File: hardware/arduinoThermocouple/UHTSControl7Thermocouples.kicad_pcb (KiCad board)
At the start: 2 copper layers, 141.6 x 63.5 mm, 71 parts, among them J1 Conn_01x12, J2 Conn_01x02, J3 Conn_01x02, J4 Conn_01x02, J5 Conn_01x02, J6 Conn_01x02, J7 Conn_01x02, J8 Conn_01x02, U1 LM317L_TO92, U2 MAX31856MUD+, U3 MAX31856MUD+, U4 MAX31856MUD+, U5 MAX31856MUD+, U6 MAX31856MUD+, U7 MAX31856MUD+, U8 MAX31856MUD+

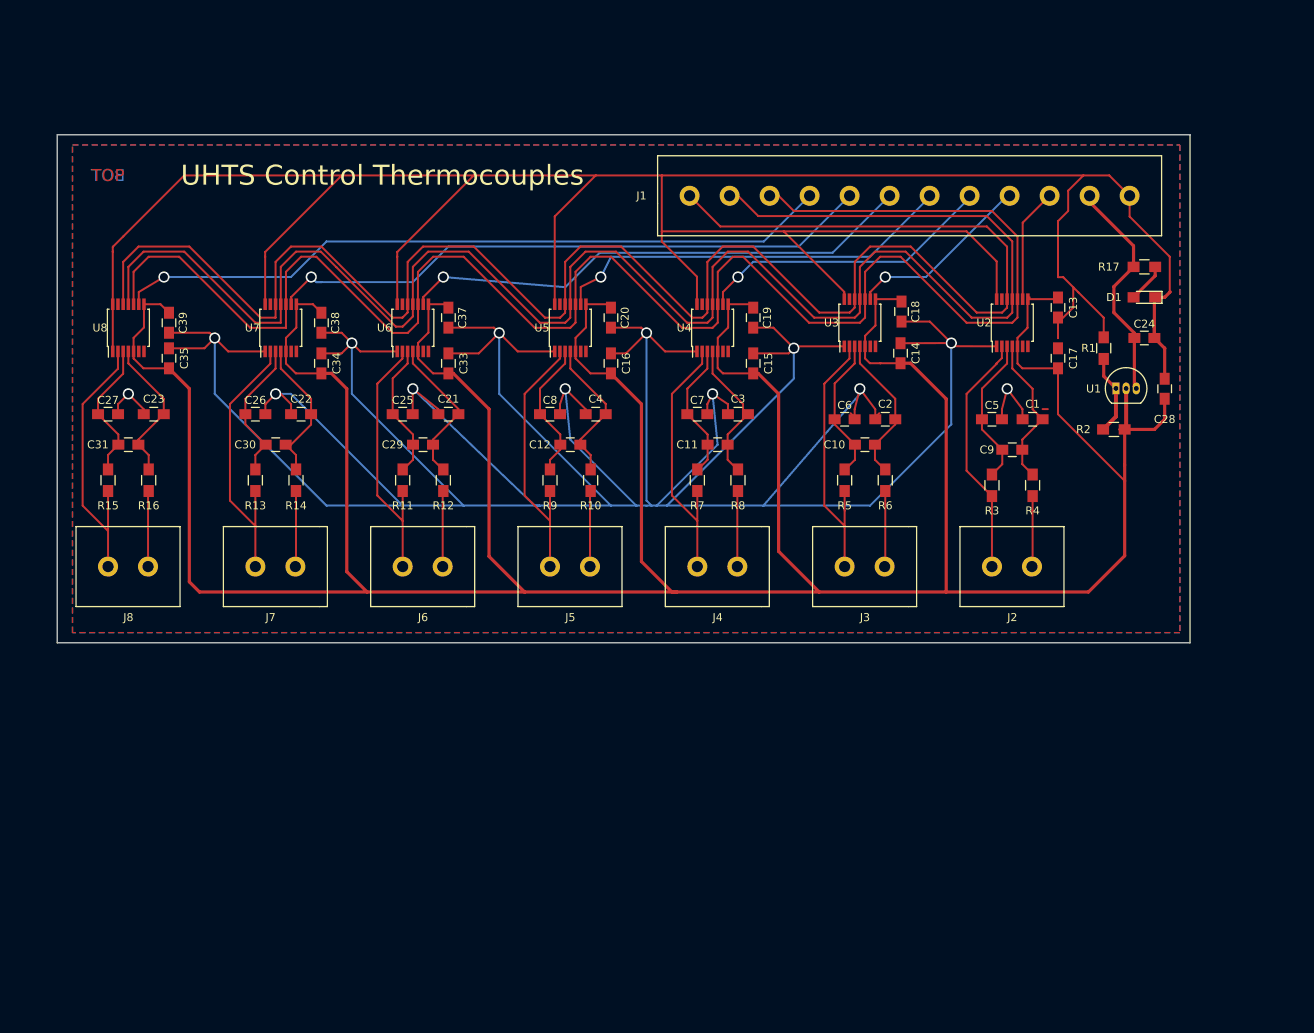
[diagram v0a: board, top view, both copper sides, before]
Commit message: Trying to learn python scripting in KiCad.
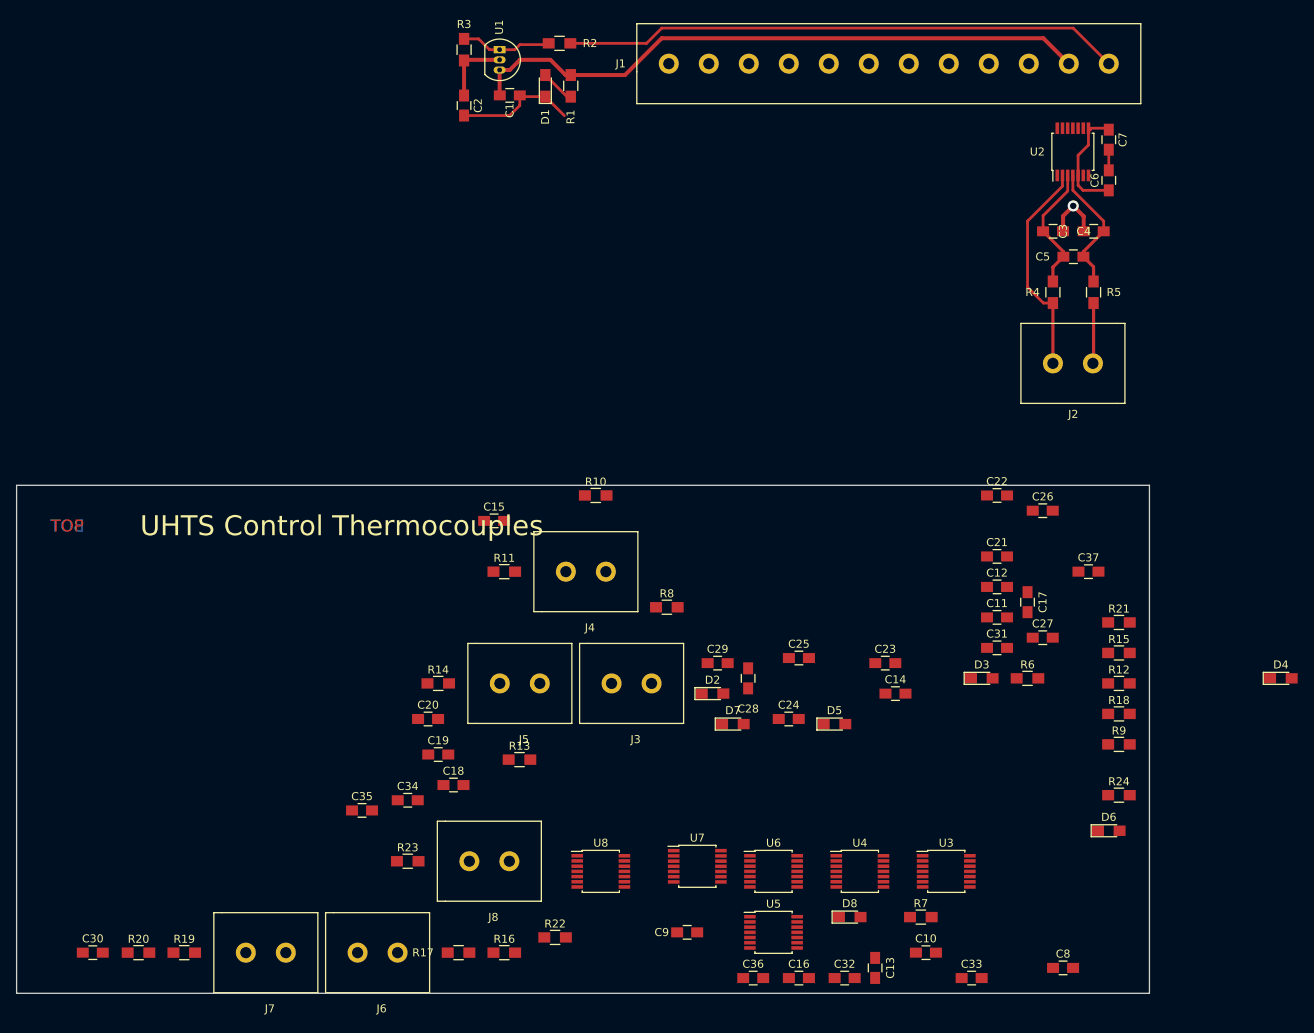
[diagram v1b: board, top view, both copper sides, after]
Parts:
- removed C38, C39: 0.1u, Capacitors_SMD:C_0805_HandSoldering
- added C32: 0.1u, Capacitors_SMD:C_0805_HandSoldering, F.Cu at (205.1, 139.1)
- added C36: 0.1u, Capacitors_SMD:C_0805_HandSoldering, F.Cu at (193.7, 139.1)
- added D2: LED, LEDs:LED_0805_HandSoldering, F.Cu at (188.6, 103.5)
- added D3: LED, LEDs:LED_0805_HandSoldering, F.Cu at (222.2, 101.6)
- added D4: LED, LEDs:LED_0805_HandSoldering, F.Cu at (259.6, 101.6)
- added D5: LED, LEDs:LED_0805_HandSoldering, F.Cu at (203.8, 107.3)
- added D6: LED, LEDs:LED_0805_HandSoldering, F.Cu at (238.1, 120.7)
- added D7: LED, LEDs:LED_0805_HandSoldering, F.Cu at (191.1, 107.3)
- added D8: LED, LEDs:LED_0805_HandSoldering, F.Cu at (205.7, 131.4)
- added R18: R, Resistors_SMD:R_0805_HandSoldering, F.Cu at (239.4, 106.0)
- added R19: 100, Resistors_SMD:R_0805_HandSoldering, F.Cu at (122.6, 135.9)
- added R20: 100, Resistors_SMD:R_0805_HandSoldering, F.Cu at (116.8, 135.9)
- added R21: R, Resistors_SMD:R_0805_HandSoldering, F.Cu at (239.4, 94.6)
- added R22: 100, Resistors_SMD:R_0805_HandSoldering, F.Cu at (168.9, 134.0)
- added R23: 100, Resistors_SMD:R_0805_HandSoldering, F.Cu at (150.5, 124.5)
- added R24: R, Resistors_SMD:R_0805_HandSoldering, F.Cu at (239.4, 116.2)
- C1: value 0.01u -> 0.1uF
- C13, C14, C18, C19, C29, C33, C34, C9: value 0.1u -> 0.01u
- C2: value 0.01u -> 1uF
- C21, C22, C25, C26, C27, C5, C6, C7: value 0.01u -> 0.1u
- C24: value 0.1uF -> 0.01u
- C28: value 1uF -> 0.01u
- R1: value 560 -> 820
- R17: value 820 -> 100
- R2: value 330 -> 560
- R3: value 100 -> 330
- moved R15 128.2 mm to (239.4, 98.4), turned to 0 degrees
- moved R17 121.2 mm to (156.8, 135.9)
- moved C27 120.1 mm to (229.9, 96.5)
- moved C31 111.5 mm to (224.2, 97.8)
- moved C33 100.9 mm to (221.0, 139.1), turned to 0 degrees
- moved C26 99.2 mm to (229.9, 80.6)
- moved C23 96.6 mm to (210.2, 99.7), turned to 0 degrees
- moved C8 94.4 mm to (232.4, 137.8)
- moved U8 90.0 mm to (174.6, 125.7), turned to 0 degrees
- moved R12 88.2 mm to (239.4, 102.2), turned to 0 degrees
- moved U1 87.9 mm to (162.0, 23.0), turned to 270 degrees
- moved C22 87.6 mm to (224.2, 78.7), turned to 0 degrees
- moved C37 86.1 mm to (235.6, 88.3), turned to 0 degrees
- moved C13 85.7 mm to (208.9, 137.8)
- moved R3 85.6 mm to (157.5, 23.0), turned to 90 degrees
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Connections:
- C1 pad 1: Net-(C1-Pad1) -> +VSW
- C11 pad 1: Net-(C11-Pad1) -> +3V3
- C11 pad 2: Net-(C11-Pad2) -> GND
- C12 pad 1: Net-(C12-Pad1) -> +3V3
- C12 pad 2: Net-(C12-Pad2) -> GND
- C13 pad 1: +3V3 -> Net-(C13-Pad1)
- C14 pad 1: +3V3 -> Net-(C14-Pad1)
- C15 pad 1: +3V3 -> Net-(C14-Pad1)
- C15 pad 2: GND -> Net-(C13-Pad1)
- C18 pad 1: +3V3 -> Net-(C18-Pad1)
- C19 pad 1: +3V3 -> Net-(C19-Pad1)
- C2 pad 1: Net-(C10-Pad2) -> +3V3
- C20 pad 1: +3V3 -> Net-(C19-Pad1)
- C20 pad 2: GND -> Net-(C18-Pad1)
- C21 pad 1: Net-(C21-Pad1) -> +3V3
- C22 pad 1: Net-(C22-Pad1) -> +3V3
- C24 pad 1: +VSW -> Net-(C24-Pad1)
- C25 pad 1: Net-(C25-Pad1) -> Net-(C24-Pad1)
- C25 pad 2: GND -> Net-(C23-Pad1)
- C26 pad 1: Net-(C26-Pad1) -> +3V3
- C27 pad 1: Net-(C27-Pad1) -> +3V3
- C28 pad 1: +3V3 -> Net-(C28-Pad1)
- C29 pad 1: Net-(C25-Pad1) -> Net-(C29-Pad1)
- C29 pad 2: Net-(C21-Pad1) -> GND
- C3 pad 1: Net-(C11-Pad2) -> Net-(C3-Pad1)
- C30 pad 1: Net-(C26-Pad1) -> Net-(C29-Pad1)
- C30 pad 2: Net-(C22-Pad1) -> Net-(C28-Pad1)
- C31 pad 1: Net-(C27-Pad1) -> +3V3
- C31 pad 2: Net-(C23-Pad1) -> GND
- C33 pad 1: +3V3 -> Net-(C33-Pad1)
- C34 pad 1: +3V3 -> Net-(C34-Pad1)
- C35 pad 1: +3V3 -> Net-(C34-Pad1)
- C35 pad 2: GND -> Net-(C33-Pad1)
- C4 pad 1: Net-(C12-Pad2) -> Net-(C4-Pad1)
- C5 pad 1: Net-(C5-Pad1) -> Net-(C4-Pad1)
- C5 pad 2: GND -> Net-(C3-Pad1)
- C6 pad 1: Net-(C10-Pad1) -> +3V3
- C7 pad 1: Net-(C11-Pad1) -> +3V3
- C8 pad 1: Net-(C12-Pad1) -> Net-(C10-Pad2)
- C9 pad 1: Net-(C5-Pad1) -> Net-(C10-Pad1)
- C9 pad 2: Net-(C1-Pad1) -> GND
- R1 pad 1: Net-(R1-Pad1) -> +VSW
- R1 pad 2: GND -> Net-(D1-Pad2)
- R10 pad 1: Net-(C12-Pad2) -> Net-(C19-Pad1)
- R10 pad 2: Net-(J5-Pad1) -> Net-(J5-Pad2)
- R11 pad 1: Net-(C25-Pad1) -> Net-(C18-Pad1)
- R11 pad 2: Net-(J6-Pad2) -> Net-(J5-Pad1)
- R12 pad 1: Net-(C21-Pad1) -> Net-(C24-Pad1)
- R12 pad 2: Net-(J6-Pad1) -> Net-(J6-Pad2)
- R13 pad 1: Net-(C26-Pad1) -> Net-(C23-Pad1)
- R13 pad 2: Net-(J7-Pad2) -> Net-(J6-Pad1)
- R14 pad 1: Net-(C22-Pad1) -> Net-(C29-Pad1)
- R14 pad 2: Net-(J7-Pad1) -> Net-(J7-Pad2)
- R15 pad 1: Net-(C27-Pad1) -> Net-(C28-Pad1)
- R15 pad 2: Net-(J8-Pad2) -> Net-(J7-Pad1)
- R16 pad 1: Net-(C23-Pad1) -> Net-(C34-Pad1)
- R16 pad 2: Net-(J8-Pad1) -> Net-(J8-Pad2)
- R17 pad 1: +VSW -> Net-(C33-Pad1)
- R17 pad 2: Net-(D1-Pad2) -> Net-(J8-Pad1)
- R2 pad 1: +3V3 -> Net-(R2-Pad1)
- R2 pad 2: Net-(R1-Pad1) -> GND
- R3 pad 1: Net-(C5-Pad1) -> +3V3
- R3 pad 2: Net-(J2-Pad2) -> Net-(R2-Pad1)
- R4 pad 1: Net-(C1-Pad1) -> Net-(C4-Pad1)
- R4 pad 2: Net-(J2-Pad1) -> Net-(J2-Pad2)
- R5 pad 1: Net-(C10-Pad1) -> Net-(C3-Pad1)
- R5 pad 2: Net-(J3-Pad2) -> Net-(J2-Pad1)
- R6 pad 1: Net-(C10-Pad2) -> Net-(C10-Pad1)
- R6 pad 2: Net-(J3-Pad1) -> Net-(J3-Pad2)
- R7 pad 1: Net-(C11-Pad1) -> Net-(C10-Pad2)
- R7 pad 2: Net-(J4-Pad2) -> Net-(J3-Pad1)
- R8 pad 1: Net-(C11-Pad2) -> Net-(C14-Pad1)
- R8 pad 2: Net-(J4-Pad1) -> Net-(J4-Pad2)
- R9 pad 1: Net-(C12-Pad1) -> Net-(C13-Pad1)
- R9 pad 2: Net-(J5-Pad2) -> Net-(J4-Pad1)
- U1 pad 1: Net-(R1-Pad1) -> Net-(R2-Pad1)
- U2 pad 3: Net-(C5-Pad1) -> Net-(C4-Pad1)
- U2 pad 4: Net-(C1-Pad1) -> Net-(C3-Pad1)
- U4 pad 3: Net-(C11-Pad1) -> Net-(C14-Pad1)
- U4 pad 4: Net-(C11-Pad2) -> Net-(C13-Pad1)
- U5 pad 3: Net-(C12-Pad1) -> Net-(C19-Pad1)
- U5 pad 4: Net-(C12-Pad2) -> Net-(C18-Pad1)
- U5 pad 9: /CS3 -> /CS4
- U6 pad 3: Net-(C25-Pad1) -> Net-(C24-Pad1)
- U6 pad 4: Net-(C21-Pad1) -> Net-(C23-Pad1)
- U6 pad 9: /CS4 -> /CS5
- U7 pad 3: Net-(C26-Pad1) -> Net-(C29-Pad1)
- U7 pad 4: Net-(C22-Pad1) -> Net-(C28-Pad1)
- U7 pad 9: /CS5 -> /CS6
- U8 pad 3: Net-(C27-Pad1) -> Net-(C34-Pad1)
- U8 pad 4: Net-(C23-Pad1) -> Net-(C33-Pad1)
- U8 pad 9: /CS6 -> /CS3
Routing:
- net GND: track 824.7 -> 95.7 mm, vias 13 -> 1
- net +3V3: track 468.1 -> 23.7 mm
- net /SDI: track 226.2 -> 0.00 mm
- net /SDO: track 221.4 -> 0.00 mm
- net /SCK: track 217.7 -> 0.00 mm
- net /CS6: track 90.1 -> 0.00 mm, vias 1 -> 0
- net /CS5: track 77.1 -> 0.00 mm, vias 1 -> 0
- net /CS4: track 65.0 -> 0.00 mm, vias 1 -> 0
- net /CS3: track 50.9 -> 0.00 mm, vias 1 -> 0
- net +VSW: track 29.5 -> 79.1 mm
- net /CS2: track 37.5 -> 0.00 mm, vias 1 -> 0
- net Net-(J8-Pad2): track 35.7 -> 0.00 mm
- net Net-(J7-Pad2): track 34.7 -> 0.00 mm
- net Net-(J3-Pad2): track 34.2 -> 0.00 mm
- net Net-(J5-Pad2): track 33.8 -> 0.00 mm
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- removed copper zone on B.Cu, net GND
- removed copper zone on F.Cu, net GND
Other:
- net class Default: clearance 0.25 -> 0.3; trace_width 0.25 -> 0.35; via_drill 1 -> 0.8
- net class IC added: clearance 0.3, trace_width 0.35, via_dia 1.4, via_drill 0.8
- net class posVOl: clearance 0.25 -> 0.3; trace_width 0.4 -> 0.5; via_drill 1 -> 0.8
- rule trace_clearance: 0.25 -> 0.3
- rule trace_min: 0.2 -> 0.25
- rule via_min_drill: 1 -> 0.8

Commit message: Trying to use KiCad with python, doesn't work on Fedora though
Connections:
- J1 pad 10: /SCK -> /CS4
- J1 pad 11: /SDO -> /CS5
- J1 pad 12: /SDI -> /CS6
- J1 pad 4: /CS1 -> /SCK
- J1 pad 5: /CS2 -> /SDO
- J1 pad 6: /CS3 -> /SDI
- J1 pad 7: /CS4 -> /CS1
- J1 pad 8: /CS5 -> /CS2
- J1 pad 9: /CS6 -> /CS3
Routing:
- net /SDI: track 0.00 -> 25.4 mm
- net /SDO: track 0.00 -> 20.2 mm
- net /SCK: track 0.00 -> 15.9 mm
- net /CS0: track 0.00 -> 11.9 mm
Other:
- net class Default: clearance 0.3 -> 0.25
- net class IC: clearance 0.3 -> 0.25
- net class SPI added: clearance 0.25, trace_width 0.325, via_dia 1.4, via_drill 0.8
- net class posVOl: clearance 0.3 -> 0.25
- rule trace_clearance: 0.3 -> 0.25
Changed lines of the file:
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@@
   (general
     (links 187)
-    (no_connects 174)
-    (area 66.92 19.439999 262.260001 144.015)
+    (no_connects 162)
+    (area 101.524999 77.394999 243.280001 141.045001)
     (thickness 1.6)
     (drawings 7)
-    (tracks 77)
+    (tracks 95)
     (zones 0)
     (modules 85)
@@
   (setup
     (last_trace_width 0.35)
-    (trace_clearance 0.3)
+    (trace_clearance 0.25)
     (zone_clearance 0.508)
     (zone_45_only no)
@@
   (net 78 "Net-(U8-Pad13)")
   (net_class Default "This is the default net class."
-    (clearance 0.3)
+    (clearance 0.25)
     (trace_width 0.35)
     (via_dia 1.4)
@@
     (uvia_dia 0.3)
     (uvia_drill 0.1)
-    (add_net /CS0)
-    (add_net /CS1)
-    (add_net /CS2)
-    (add_net /CS3)
-    (add_net /CS4)
-    (add_net /CS5)
-    (add_net /CS6)
-    (add_net /SCK)
-    (add_net /SDI)
-    (add_net /SDO)
     (add_net GND)
   )
   (net_class IC ""
-    (clearance 0.3)
+    (clearance 0.25)
     (trace_width 0.35)
     (via_dia 1.4)
@@
     (add_net "Net-(U8-Pad7)")
   )
+  (net_class SPI ""
+    (clearance 0.25)
+    (trace_width 0.325)
+    (via_dia 1.4)
+    (via_drill 0.8)
+    (uvia_dia 0.3)
+    (uvia_drill 0.1)
+    (add_net /CS0)
+    (add_net /CS1)
+    (add_net /CS2)
+    (add_net /CS3)
+    (add_net /CS4)
+    (add_net /CS5)
+    (add_net /CS6)
+    (add_net /SCK)
+    (add_net /SDI)
+    (add_net /SDO)
+  )
   (net_class posVOl ""
-    (clearance 0.3)
+    (clearance 0.25)
     (trace_width 0.5)
     (via_dia 1.4)
@@
       (net 11 /CS0))
     (pad 4 thru_hole circle (at -13 0 180) (size 2.5 2.5) (drill 1.4) (layers *.Cu *.Mask)
-      (net 12 /CS1))
+      (net 10 /SCK))
     (pad 5 thru_hole circle (at -8 0 180) (size 2.5 2.5) (drill 1.4) (layers *.Cu *.Mask)
-      (net 13 /CS2))
+      (net 9 /SDO))
     (pad 6 thru_hole circle (at -3 0 180) (size 2.5 2.5) (drill 1.4) (layers *.Cu *.Mask)
-      (net 14 /CS3))
+      (net 8 /SDI))
     (pad 7 thru_hole circle (at 2 0 180) (size 2.5 2.5) (drill 1.4) (layers *.Cu *.Mask)
-      (net 15 /CS4))
+      (net 12 /CS1))
     (pad 8 thru_hole circle (at 7 0 180) (size 2.5 2.5) (drill 1.4) (layers *.Cu *.Mask)
-      (net 16 /CS5))
+      (net 13 /CS2))
     (pad 9 thru_hole circle (at 12 0 180) (size 2.5 2.5) (drill 1.4) (layers *.Cu *.Mask)
-      (net 17 /CS6))
+      (net 14 /CS3))
     (pad 10 thru_hole circle (at 17 0 180) (size 2.5 2.5) (drill 1.4) (layers *.Cu *.Mask)
-      (net 10 /SCK))
+      (net 15 /CS4))
     (pad 11 thru_hole circle (at 22 0 180) (size 2.5 2.5) (drill 1.4) (layers *.Cu *.Mask)
-      (net 9 /SDO))
+      (net 16 /CS5))
     (pad 12 thru_hole circle (at 27 0 180) (size 2.5 2.5) (drill 1.4) (layers *.Cu *.Mask)
-      (net 8 /SDI))
+      (net 17 /CS6))
   )
   (module Capacitors_SMD:C_0805_HandSoldering placed (layer F.Cu)
@@
   (via (at 233.68 42.545) (size 1.4) (drill 0.8) (layers F.Cu B.Cu) (net 1))
   (segment (start 234.99 45.72) (end 234.99 43.855) (width 0.5) (layer F.Cu) (net 1))
+  (segment (start 235.585 34.925) (end 235.585 32.835) (width 0.35) (layer F.Cu) (net 4))
+  (segment (start 238.125 33.02) (end 235.77 33.02) (width 0.5) (layer F.Cu) (net 4))
+  (segment (start 235.77 33.02) (end 235.710001 32.960001) (width 0.5) (layer F.Cu) (net 4))
   (segment (start 157.532683 24.366777) (end 157.532683 28.751777) (width 0.5) (layer F.Cu) (net 4))
   (segment (start 161.977683 24.286777) (end 157.612683 24.286777) (width 0.5) (layer F.Cu) (net 4))
   (segment (start 157.612683 24.286777) (end 157.532683 24.366777) (width 0.5) (layer F.Cu) (net 4))
   (segment (start 161.897683 24.366777) (end 161.977683 24.286777) (width 0.35) (layer F.Cu) (net 4))
-  (segment (start 235.585 32.835) (end 235.585 34.925) (width 0.35) (layer F.Cu) (net 4))
   (segment (start 235.585 34.925) (end 234.285 36.225) (width 0.35) (layer F.Cu) (net 4))
   (segment (start 234.285 36.225) (end 234.285 38.735) (width 0.35) (layer F.Cu) (net 4))
-  (segment (start 235.585 32.835) (end 237.94 32.835) (width 0.35) (layer F.Cu) (net 4))
   (segment (start 237.94 32.835) (end 238.125 33.02) (width 0.35) (layer F.Cu) (net 4))
-  (segment (start 235.81 33.06) (end 235.585 32.835) (width 0.35) (layer F.Cu) (net 4))
   (segment (start 234.91 40.6) (end 234.285 39.975) (width 0.35) (layer F.Cu) (net 4))
   (segment (start 234.285 39.975) (end 234.285 38.735) (width 0.35) (layer F.Cu) (net 4))
@@
   (segment (start 170.867683 28.886777) (end 170.392683 28.886777) (width 0.35) (layer F.Cu) (net 7))
   (segment (start 170.392683 28.886777) (end 167.692683 26.186777) (width 0.35) (layer F.Cu) (net 7))
+  (segment (start 213.125 24.765) (end 213.125 26.532766) (width 0.325) (layer F.Cu) (net 8))
+  (segment (start 232.985 30.776372) (end 232.985 32.835) (width 0.325) (layer F.Cu) (net 8))
+  (segment (start 213.125 26.532766) (end 214.169755 27.577521) (width 0.325) (layer F.Cu) (net 8))
+  (segment (start 214.169755 27.577521) (end 229.786149 27.577521) (width 0.325) (layer F.Cu) (net 8))
+  (segment (start 229.786149 27.577521) (end 232.985 30.776372) (width 0.325) (layer F.Cu) (net 8))
+  (segment (start 218.125 24.765) (end 220.362511 27.002511) (width 0.325) (layer F.Cu) (net 9))
+  (segment (start 220.362511 27.002511) (end 230.024325 27.002511) (width 0.325) (layer F.Cu) (net 9))
+  (segment (start 230.024325 27.002511) (end 233.635 30.613186) (width 0.325) (layer F.Cu) (net 9))
+  (segment (start 233.635 30.613186) (end 233.635 32.835) (width 0.325) (layer F.Cu) (net 9))
+  (segment (start 233.647499 32.822501) (end 233.635 32.835) (width 0.325) (layer F.Cu) (net 9))
+  (segment (start 230.262501 26.427501) (end 234.285 30.45) (width 0.325) (layer F.Cu) (net 10))
+  (segment (start 224.787501 26.427501) (end 230.262501 26.427501) (width 0.325) (layer F.Cu) (net 10))
+  (segment (start 223.125 24.765) (end 224.787501 26.427501) (width 0.325) (layer F.Cu) (net 10))
+  (segment (start 234.285 30.45) (end 234.285 32.835) (width 0.325) (layer F.Cu) (net 10))
+  (segment (start 228.125 24.765) (end 229.892766 24.765) (width 0.325) (layer F.Cu) (net 11))
+  (segment (start 229.892766 24.765) (end 234.935 29.807234) (width 0.325) (layer F.Cu) (net 11))
+  (segment (start 234.935 29.807234) (end 234.935 31.785) (width 0.325) (layer F.Cu) (net 11))
+  (segment (start 234.935 31.785) (end 234.935 32.835) (width 0.325) (layer F.Cu) (net 11))
   (segment (start 236.22 54.69) (end 236.22 62.15) (width 0.4) (layer F.Cu) (net 18))
   (segment (start 236.22 62.15) (end 236.14 62.23) (width 0.4) (layer F.Cu) (net 18))
